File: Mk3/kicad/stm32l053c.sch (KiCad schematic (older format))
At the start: 39 parts, among them J1 GND, J2 GND, J3 TX, J4 GND, J5 TEST_1P, J6 TEST_1P, J7 TEST_1P, P1 SWD, U1 AP2112, U2 STM32L053C8_LQFP48, U3 ADS1015, U4 UFL_SMA, U5 RFM92/95

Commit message: Extra battery pins
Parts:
- BT1: footprint theapi:BatteryBox -> theapi:BatteryBoxAndPins
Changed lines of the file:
@@
 F 0 "BT1" H 2700 1575 50  0000 L CNN
 F 1 "Battery" H 2700 1475 50  0000 L CNN
-F 2 "theapi:BatteryBox" V 2600 1535 50  0001 C CNN
+F 2 "theapi:BatteryBoxAndPins" V 2600 1535 50  0001 C CNN
 F 3 "" V 2600 1535 50  0001 C CNN
 	1    2600 1475

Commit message: Serial RX
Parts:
- added J8: RX, Pin_Headers:Pin_Header_Straight_1x01_Pitch2.54mm, symbol CONN_01X01
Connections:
- net USART1_RX: now reaches U2.31 (PA10)
- net USART1_RX: now also J8.1 (P1)
- no-connect marks 11 -> 10
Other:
- moved on the sheet: D1, J1, J2, J3, J4, R1

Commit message: An extra capacitor
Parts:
- added C9: 10uF, Capacitors_SMD:C_0805_HandSoldering, symbol C
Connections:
- net +3V3: now also C9.1
- net Earth: now also C9.2
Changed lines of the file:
@@
 	3750 1875 3750 1925
 Wire Wire Line
-	3050 1925 4450 1925
+	3050 1925 4750 1925
 Wire Wire Line
 	3050 1925 3050 1775
 Wire Wire Line
-	4150 1475 4450 1475
+	4150 1475 4750 1475
 Wire Wire Line
 	4450 1475 4450 1175
@@
 	-1   0    0    1
 $EndComp
+$Comp
+L C C9
+U 1 1 59466076
+P 4750 1625
+F 0 "C9" H 4775 1725 50  0000 L CNN
+F 1 "10uF" H 4775 1525 50  0000 L CNN
+F 2 "Capacitors_SMD:C_0805_HandSoldering" H 4788 1475 50  0001 C CNN
+F 3 "" H 4750 1625 50  0000 C CNN
+	1    4750 1625
+	1    0    0    -1
+$EndComp
+Wire Wire Line
+	4750 1925 4750 1775
+Connection ~ 4450 1925
+Connection ~ 4450 1475
 $EndSCHEMATC

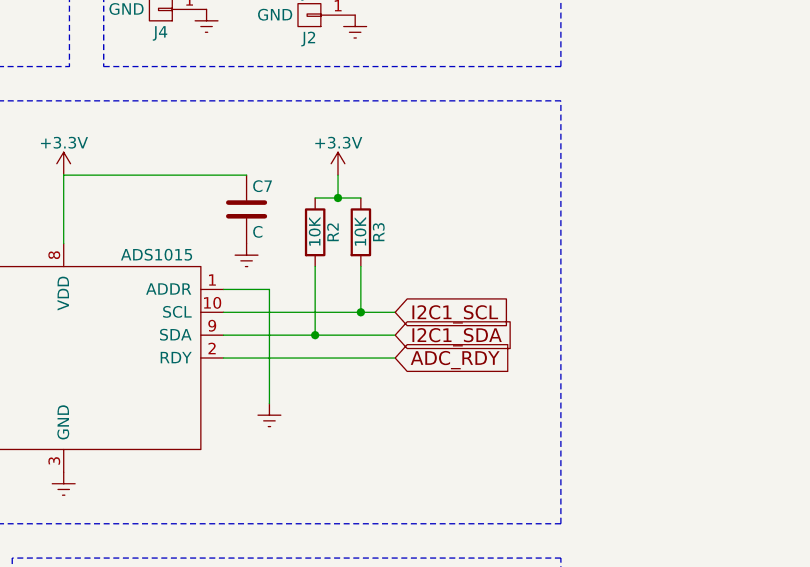
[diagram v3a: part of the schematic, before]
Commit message: Pullup on ADC RDY pin
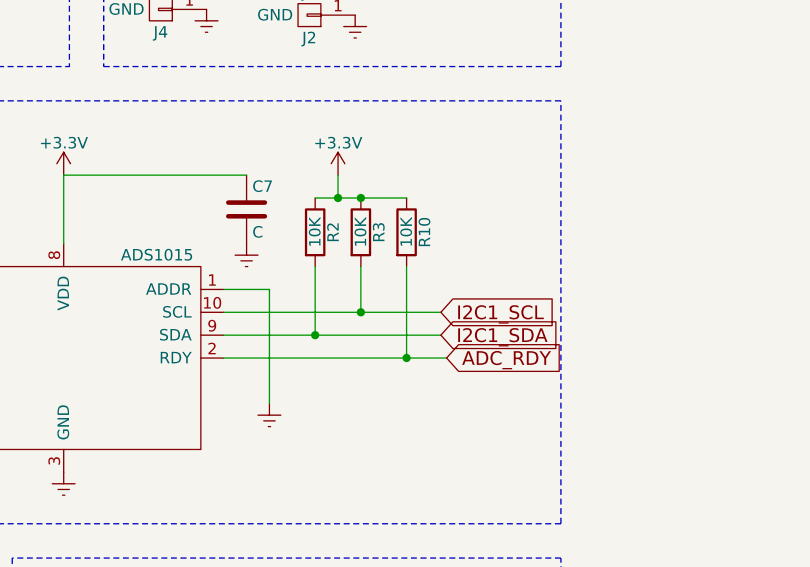
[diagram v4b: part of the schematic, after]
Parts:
- added R10: 10K, Resistors_SMD:R_0805_HandSoldering, symbol R
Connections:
- net +3V3: now also R10.1
- net ADC_RDY: now also R10.2
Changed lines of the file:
@@
 $EndDescr
 $Comp
-L Earth #PWR28
+L Earth #PWR8
 U 1 1 58021BE1
 P 7400 1900
-F 0 "#PWR28" H 7400 1650 50  0001 C CNN
+F 0 "#PWR8" H 7400 1650 50  0001 C CNN
 F 1 "Earth" H 7400 1750 50  0001 C CNN
 F 2 "" H 7400 1900 50  0000 C CNN
@@
 $EndComp
 $Comp
-L GNDA #PWR33
+L GNDA #PWR25
 U 1 1 58021F75
 P 9325 5925
-F 0 "#PWR33" H 9325 5675 50  0001 C CNN
+F 0 "#PWR25" H 9325 5675 50  0001 C CNN
 F 1 "GNDA" H 9325 5775 50  0000 C CNN
 F 2 "" H 9325 5925 50  0000 C CNN
@@
 $EndComp
 $Comp
-L Earth #PWR34
+L Earth #PWR26
 U 1 1 58021F89
 P 9825 5925
-F 0 "#PWR34" H 9825 5675 50  0001 C CNN
+F 0 "#PWR26" H 9825 5675 50  0001 C CNN
 F 1 "Earth" H 9825 5775 50  0001 C CNN
 F 2 "" H 9825 5925 50  0000 C CNN
@@
 $EndComp
 $Comp
-L GNDA #PWR30
+L GNDA #PWR27
 U 1 1 58022154
 P 8175 5950
-F 0 "#PWR30" H 8175 5700 50  0001 C CNN
+F 0 "#PWR27" H 8175 5700 50  0001 C CNN
 F 1 "GNDA" H 8175 5800 50  0000 C CNN
 F 2 "" H 8175 5950 50  0000 C CNN
@@
 $EndComp
 $Comp
-L Earth #PWR32
+L Earth #PWR28
 U 1 1 580221FA
 P 8675 5950
-F 0 "#PWR32" H 8675 5700 50  0001 C CNN
+F 0 "#PWR28" H 8675 5700 50  0001 C CNN
 F 1 "Earth" H 8675 5800 50  0001 C CNN
 F 2 "" H 8675 5950 50  0000 C CNN
@@
 $EndComp
 $Comp
-L Earth #PWR7
+L Earth #PWR13
 U 1 1 580369A9
 P 2425 3075
-F 0 "#PWR7" H 2425 2825 50  0001 C CNN
+F 0 "#PWR13" H 2425 2825 50  0001 C CNN
 F 1 "Earth" H 2425 2925 50  0001 C CNN
 F 2 "" H 2425 3075 50  0000 C CNN
@@
 NRST
 $Comp
-L Earth #PWR25
+L Earth #PWR6
 U 1 1 58039244
 P 6675 1900
-F 0 "#PWR25" H 6675 1650 50  0001 C CNN
+F 0 "#PWR6" H 6675 1650 50  0001 C CNN
 F 1 "Earth" H 6675 1750 50  0001 C CNN
 F 2 "" H 6675 1900 50  0000 C CNN
@@
 $EndComp
 $Comp
-L Earth #PWR26
+L Earth #PWR7
 U 1 1 5803BDC8
 P 7050 1900
-F 0 "#PWR26" H 7050 1650 50  0001 C CNN
+F 0 "#PWR7" H 7050 1650 50  0001 C CNN
 F 1 "Earth" H 7050 1750 50  0001 C CNN
 F 2 "" H 7050 1900 50  0000 C CNN
@@
 $EndComp
 $Comp
-L Earth #PWR27
+L Earth #PWR21
 U 1 1 58065816
 P 7275 4950
-F 0 "#PWR27" H 7275 4700 50  0001 C CNN
+F 0 "#PWR21" H 7275 4700 50  0001 C CNN
 F 1 "Earth" H 7275 4800 50  0001 C CNN
 F 2 "" H 7275 4950 50  0000 C CNN
@@
 $EndComp
 $Comp
-L Earth #PWR15
+L Earth #PWR11
 U 1 1 58077163
 P 3550 2800
-F 0 "#PWR15" H 3550 2550 50  0001 C CNN
+F 0 "#PWR11" H 3550 2550 50  0001 C CNN
 F 1 "Earth" H 3550 2650 50  0001 C CNN
 F 2 "" H 3550 2800 50  0000 C CNN
@@
 Place on Top layer
 $Comp
-L Earth #PWR11
+L Earth #PWR23
 U 1 1 592DF55A
 P 2900 5450
-F 0 "#PWR11" H 2900 5200 50  0001 C CNN
+F 0 "#PWR23" H 2900 5200 50  0001 C CNN
 F 1 "Earth" H 2900 5300 50  0001 C CNN
 F 2 "" H 2900 5450 50  0000 C CNN
@@
 NoConn ~ 4150 1625
 $Comp
-L Earth #PWR17
+L Earth #PWR10
 U 1 1 592F1C89
 P 3750 1925
-F 0 "#PWR17" H 3750 1675 50  0001 C CNN
+F 0 "#PWR10" H 3750 1675 50  0001 C CNN
 F 1 "Earth" H 3750 1775 50  0001 C CNN
 F 2 "" H 3750 1925 50  0000 C CNN
@@
 Text GLabel 9575 3050 2    60   Input ~ 0
 I2C1_SCL
-Text GLabel 4350 4750 2    60   Input ~ 0
+Text GLabel 4550 4750 2    60   Input ~ 0
 I2C1_SCL
-Text GLabel 4350 4850 2    60   Input ~ 0
+Text GLabel 4550 4850 2    60   Input ~ 0
 I2C1_SDA
 Text GLabel 9575 3950 2    60   Input ~ 0
@@
 RFM_RST
 $Comp
-L +3.3V #PWR21
+L +3.3V #PWR1
 U 1 1 592F43A5
 P 4450 1175
-F 0 "#PWR21" H 4450 1025 50  0001 C CNN
+F 0 "#PWR1" H 4450 1025 50  0001 C CNN
 F 1 "+3.3V" H 4450 1315 50  0000 C CNN
 F 2 "" H 4450 1175 50  0001 C CNN
@@
 $EndComp
 $Comp
-L +3.3V #PWR5
+L +3.3V #PWR12
 U 1 1 592F4BC3
 P 1925 2875
-F 0 "#PWR5" H 1925 2725 50  0001 C CNN
+F 0 "#PWR12" H 1925 2725 50  0001 C CNN
 F 1 "+3.3V" H 1925 3015 50  0000 C CNN
 F 2 "" H 1925 2875 50  0001 C CNN
@@
 $EndComp
 $Comp
-L +3.3V #PWR31
+L +3.3V #PWR2
 U 1 1 592F4E66
 P 8475 1425
-F 0 "#PWR31" H 8475 1275 50  0001 C CNN
+F 0 "#PWR2" H 8475 1275 50  0001 C CNN
 F 1 "+3.3V" H 8475 1565 50  0000 C CNN
 F 2 "" H 8475 1425 50  0001 C CNN
@@
 $EndComp
 $Comp
-L +3.3V #PWR22
+L +3.3V #PWR32
 U 1 1 592F53D7
 P 4775 6725
-F 0 "#PWR22" H 4775 6575 50  0001 C CNN
+F 0 "#PWR32" H 4775 6575 50  0001 C CNN
 F 1 "+3.3V" H 4775 6865 50  0000 C CNN
 F 2 "" H 4775 6725 50  0001 C CNN
@@
 $EndComp
 $Comp
-L +3.3V #PWR24
+L +3.3V #PWR3
 U 1 1 592F54CD
 P 6675 1600
-F 0 "#PWR24" H 6675 1450 50  0001 C CNN
+F 0 "#PWR3" H 6675 1450 50  0001 C CNN
 F 1 "+3.3V" H 6675 1740 50  0000 C CNN
 F 2 "" H 6675 1600 50  0001 C CNN
@@
 NoConn ~ 7625 3550
 $Comp
-L Earth #PWR23
+L Earth #PWR33
 U 1 1 592F7C8A
 P 4775 7025
-F 0 "#PWR23" H 4775 6775 50  0001 C CNN
+F 0 "#PWR33" H 4775 6775 50  0001 C CNN
 F 1 "Earth" H 4775 6875 50  0001 C CNN
 F 2 "" H 4775 7025 50  0000 C CNN
@@
 $EndComp
 $Comp
-L Earth #PWR9
+L Earth #PWR29
 U 1 1 592F7CF0
 P 2750 6425
-F 0 "#PWR9" H 2750 6175 50  0001 C CNN
+F 0 "#PWR29" H 2750 6175 50  0001 C CNN
 F 1 "Earth" H 2750 6275 50  0001 C CNN
 F 2 "" H 2750 6425 50  0000 C CNN
@@
 $EndComp
 $Comp
-L Earth #PWR12
+L Earth #PWR34
 U 1 1 592F7EE4
 P 3225 7125
-F 0 "#PWR12" H 3225 6875 50  0001 C CNN
+F 0 "#PWR34" H 3225 6875 50  0001 C CNN
 F 1 "Earth" H 3225 6975 50  0001 C CNN
 F 2 "" H 3225 7125 50  0000 C CNN
@@
 $EndComp
 $Comp
-L Earth #PWR2
+L Earth #PWR30
 U 1 1 592F80DC
 P 1300 6575
-F 0 "#PWR2" H 1300 6325 50  0001 C CNN
+F 0 "#PWR30" H 1300 6325 50  0001 C CNN
 F 1 "Earth" H 1300 6425 50  0001 C CNN
 F 2 "" H 1300 6575 50  0000 C CNN
@@
 $EndComp
 $Comp
-L Earth #PWR6
+L Earth #PWR31
 U 1 1 592F814F
 P 2050 6600
-F 0 "#PWR6" H 2050 6350 50  0001 C CNN
+F 0 "#PWR31" H 2050 6350 50  0001 C CNN
 F 1 "Earth" H 2050 6450 50  0001 C CNN
 F 2 "" H 2050 6600 50  0000 C CNN
@@
 $EndComp
 $Comp
-L Earth #PWR18
+L Earth #PWR22
 U 1 1 59301904
 P 3800 5150
-F 0 "#PWR18" H 3800 4900 50  0001 C CNN
+F 0 "#PWR22" H 3800 4900 50  0001 C CNN
 F 1 "Earth" H 3800 5000 50  0001 C CNN
 F 2 "" H 3800 5150 50  0000 C CNN
@@
 	-1   0    0    -1
 $EndComp
-Text GLabel 4350 4950 2    60   Input ~ 0
+Text GLabel 4575 4950 2    60   Input ~ 0
 ADC_RDY
 Text GLabel 9575 3350 2    60   Input ~ 0
@@
 $EndComp
 $Comp
-L Earth #PWR16
+L Earth #PWR19
 U 1 1 593024E3
 P 3700 4450
-F 0 "#PWR16" H 3700 4200 50  0001 C CNN
+F 0 "#PWR19" H 3700 4200 50  0001 C CNN
 F 1 "Earth" H 3700 4300 50  0001 C CNN
 F 2 "" H 3700 4450 50  0000 C CNN
@@
 $EndComp
 $Comp
-L +3.3V #PWR10
+L +3.3V #PWR17
 U 1 1 59303669
 P 2900 4150
-F 0 "#PWR10" H 2900 4000 50  0001 C CNN
+F 0 "#PWR17" H 2900 4000 50  0001 C CNN
 F 1 "+3.3V" H 2900 4290 50  0000 C CNN
 F 2 "" H 2900 4150 50  0001 C CNN
@@
 $EndComp
 $Comp
-L +3.3V #PWR19
+L +3.3V #PWR18
 U 1 1 59303771
 P 4100 4150
-F 0 "#PWR19" H 4100 4000 50  0001 C CNN
+F 0 "#PWR18" H 4100 4000 50  0001 C CNN
 F 1 "+3.3V" H 4100 4290 50  0000 C CNN
 F 2 "" H 4100 4150 50  0001 C CNN
@@
 $EndComp
 $Comp
-L Earth #PWR8
+L Earth #PWR4
 U 1 1 59316863
 P 2600 1675
-F 0 "#PWR8" H 2600 1425 50  0001 C CNN
+F 0 "#PWR4" H 2600 1425 50  0001 C CNN
 F 1 "Earth" H 2600 1525 50  0001 C CNN
 F 2 "" H 2600 1675 50  0000 C CNN
@@
 $EndComp
 $Comp
-L Earth #PWR1
+L Earth #PWR20
 U 1 1 593290F6
 P 1275 4775
-F 0 "#PWR1" H 1275 4525 50  0001 C CNN
+F 0 "#PWR20" H 1275 4525 50  0001 C CNN
 F 1 "Earth" H 1275 4625 50  0001 C CNN
 F 2 "" H 1275 4775 50  0000 C CNN
@@
 $EndComp
 $Comp
-L Earth #PWR3
+L Earth #PWR5
 U 1 1 59355822
 P 1650 1900
-F 0 "#PWR3" H 1650 1650 50  0001 C CNN
+F 0 "#PWR5" H 1650 1650 50  0001 C CNN
 F 1 "Earth" H 1650 1750 50  0001 C CNN
 F 2 "" H 1650 1900 50  0000 C CNN
@@
 $EndComp
 $Comp
-L Earth #PWR4
+L Earth #PWR24
 U 1 1 59357323
 P 1900 5500
-F 0 "#PWR4" H 1900 5250 50  0001 C CNN
+F 0 "#PWR24" H 1900 5250 50  0001 C CNN
 F 1 "Earth" H 1900 5350 50  0001 C CNN
 F 2 "" H 1900 5500 50  0000 C CNN
@@
 $EndComp
 $Comp
-L Earth #PWR29
+L Earth #PWR9
 U 1 1 59375C9C
 P 7700 1900
-F 0 "#PWR29" H 7700 1650 50  0001 C CNN
+F 0 "#PWR9" H 7700 1650 50  0001 C CNN
 F 1 "Earth" H 7700 1750 50  0001 C CNN
 F 2 "" H 7700 1900 50  0000 C CNN
@@
 	3400 6425 2750 6425
 Wire Wire Line
-	3600 4750 4350 4750
-Wire Wire Line
-	3600 4850 4350 4850
+	3600 4750 4550 4750
+Wire Wire Line
+	3600 4850 4550 4850
 Wire Wire Line
 	4000 4550 4000 4850
@@
 Connection ~ 4200 4750
 Wire Wire Line
-	4000 4250 4200 4250
+	4000 4250 4400 4250
 Connection ~ 4100 4250
 Wire Wire Line
@@
 	3800 4650 3600 4650
 Wire Wire Line
-	4350 4950 3600 4950
+	4575 4950 3600 4950
 Wire Wire Line
 	3750 1875 3750 1925
@@
 $EndComp
 $Comp
-L Earth #PWR20
+L Earth #PWR16
 U 1 1 59379ABF
 P 4175 3450
-F 0 "#PWR20" H 4175 3200 50  0001 C CNN
+F 0 "#PWR16" H 4175 3200 50  0001 C CNN
 F 1 "Earth" H 4175 3300 50  0001 C CNN
 F 2 "" H 4175 3450 50  0000 C CNN
@@
 $EndComp
 $Comp
-L Earth #PWR14
+L Earth #PWR15
 U 1 1 593AA95B
 P 3525 3425
-F 0 "#PWR14" H 3525 3175 50  0001 C CNN
+F 0 "#PWR15" H 3525 3175 50  0001 C CNN
 F 1 "Earth" H 3525 3275 50  0001 C CNN
 F 2 "" H 3525 3425 50  0000 C CNN
@@
 $EndComp
 $Comp
-L Earth #PWR13
+L Earth #PWR14
 U 1 1 593AA9D2
 P 3525 3175
-F 0 "#PWR13" H 3525 2925 50  0001 C CNN
+F 0 "#PWR14" H 3525 2925 50  0001 C CNN
 F 1 "Earth" H 3525 3025 50  0001 C CNN
 F 2 "" H 3525 3175 50  0000 C CNN
@@
 Connection ~ 4450 1925
 Connection ~ 4450 1475
+$Comp
+L R R10
+U 1 1 59492AEA
+P 4400 4400
+F 0 "R10" V 4480 4400 50  0000 C CNN
+F 1 "10K" V 4400 4400 50  0000 C CNN
+F 2 "Resistors_SMD:R_0805_HandSoldering" V 4330 4400 50  0001 C CNN
+F 3 "" H 4400 4400 50  0001 C CNN
+	1    4400 4400
+	1    0    0    -1
+$EndComp
+Wire Wire Line
+	4400 4550 4400 4950
+Connection ~ 4400 4950
+Connection ~ 4200 4250
 $EndSCHEMATC
